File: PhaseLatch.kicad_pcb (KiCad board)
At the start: 4 copper layers, 68.8 x 53.6 mm, 120 parts, among them J2 NC, J20 I_IN, J21 Q_IN, J23 CLK_IN, J5 Databus, J6 Chip select, J7 Addressbus, J8 Signals, P1 Conn_02x10_Odd_Even, P2 Conn_02x10_Odd_Even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

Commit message: Ready for review
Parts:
- added C25: 100nF, Capacitor_SMD:C_0402_1005Metric, F.Cu at (170.2, 104.6)
- added C26: 100nF, Capacitor_SMD:C_0402_1005Metric, F.Cu at (149.4, 134.1)
- added C27: 100nF, Capacitor_SMD:C_0402_1005Metric, F.Cu at (139.2, 130.0)
- U2, U6, U7, U8: value TP74LVC1G132S5 -> SN74LVC1G132DCKR; footprint Package_TO_SOT_SMD:SOT-23-5 -> Package_TO_SOT_SMD:SOT-353_SC-70-5
- moved C21 20.9 mm to (155.5, 127.1)
- moved R26 1.44 mm to (142.0, 116.6), turned to -90 degrees
- moved C19 1.28 mm to (146.2, 119.8)
- moved R16 1.25 mm to (146.2, 120.8)
- moved C9 1.22 mm to (143.3, 119.3)
- moved R46 1.21 mm to (163.6, 112.5)
- moved R45 1.19 mm to (163.6, 113.4)
- moved R42 1.16 mm to (163.6, 116.2)
- moved R44 1.16 mm to (163.6, 114.3)
- moved R41 1.15 mm to (163.6, 117.2)
- moved R39 1.14 mm to (163.6, 119.1)
- moved R40 1.14 mm to (163.6, 118.2)
- moved R43 1.14 mm to (163.6, 115.3)
- moved C4 1.06 mm to (140.8, 120.2)
- moved C5 1.01 mm to (140.8, 119.2)
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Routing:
- net /"$0800": track 0.00 -> 35.5 mm, vias 0 -> 2
- net Net-(JP9-A): track 15.5 -> 37.9 mm
- net Net-(JP14-B): track 0.00 -> 21.0 mm, vias 0 -> 2
- net VCC: track 17.1 -> 33.7 mm, vias 12 -> 15
- net Net-(U4-~{OE}): track 5.51 -> 19.8 mm
- net +Ext_3V3: track 55.0 -> 69.2 mm
- net A6: track 55.6 -> 68.0 mm
- net GND: track 0.00 -> 7.29 mm, vias 42 -> 110
- net Net-(JP14-A): track 11.9 -> 14.6 mm
- net Net-(JP6-A): track 5.06 -> 7.39 mm
- net /PB2: track 20.7 -> 22.6 mm
- net Net-(JP6-B): track 17.7 -> 19.5 mm
- net Net-(U1-D1): track 3.13 -> 1.68 mm
- net Net-(U1-REFT-I): track 6.56 -> 8.00 mm
- net Net-(U1-D0): track 3.29 -> 1.87 mm
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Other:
- board text added: "A0"
- board text added: "A13"
- board text added: "A14"
- board text added: "CLK"

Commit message: Mods from review
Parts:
- moved JP4 0.89 mm to (164.8, 134.2)
- moved JP5 0.85 mm to (164.8, 132.2)
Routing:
- net A6: track 68.0 -> 51.6 mm, vias 1 -> 2
- net D2: track 46.6 -> 49.2 mm
- net D1: track 49.9 -> 51.8 mm
- net VCC: track 33.7 -> 32.2 mm
- net Net-(U4-~{WE}): track 28.8 -> 30.4 mm
- net Net-(JP2-B): track 16.1 -> 14.8 mm
- net D3: track 51.9 -> 53.1 mm
- net A0: track 58.4 -> 59.4 mm
- net /PB2: track 22.6 -> 21.6 mm
- net D5: track 50.7 -> 49.7 mm
- net Net-(JP5-A): track 2.87 -> 2.02 mm
- net /A13: track 99.3 -> 100.0 mm
- net D0: track 47.1 -> 47.6 mm
- net GND: vias 110 -> 144

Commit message: Final touches
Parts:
- moved C21 4.72 mm to (150.8, 126.9)
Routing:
- net Net-(U4-~{WE}): track 30.4 -> 27.7 mm
- net /A13: track 100.0 -> 98.2 mm
- net VCC: track 32.2 -> 33.9 mm
- net Net-(JP1-C): track 4.66 -> 5.40 mm
- net GND: vias 144 -> 168
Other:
- board text added: "S"
- board text added: "VDD"

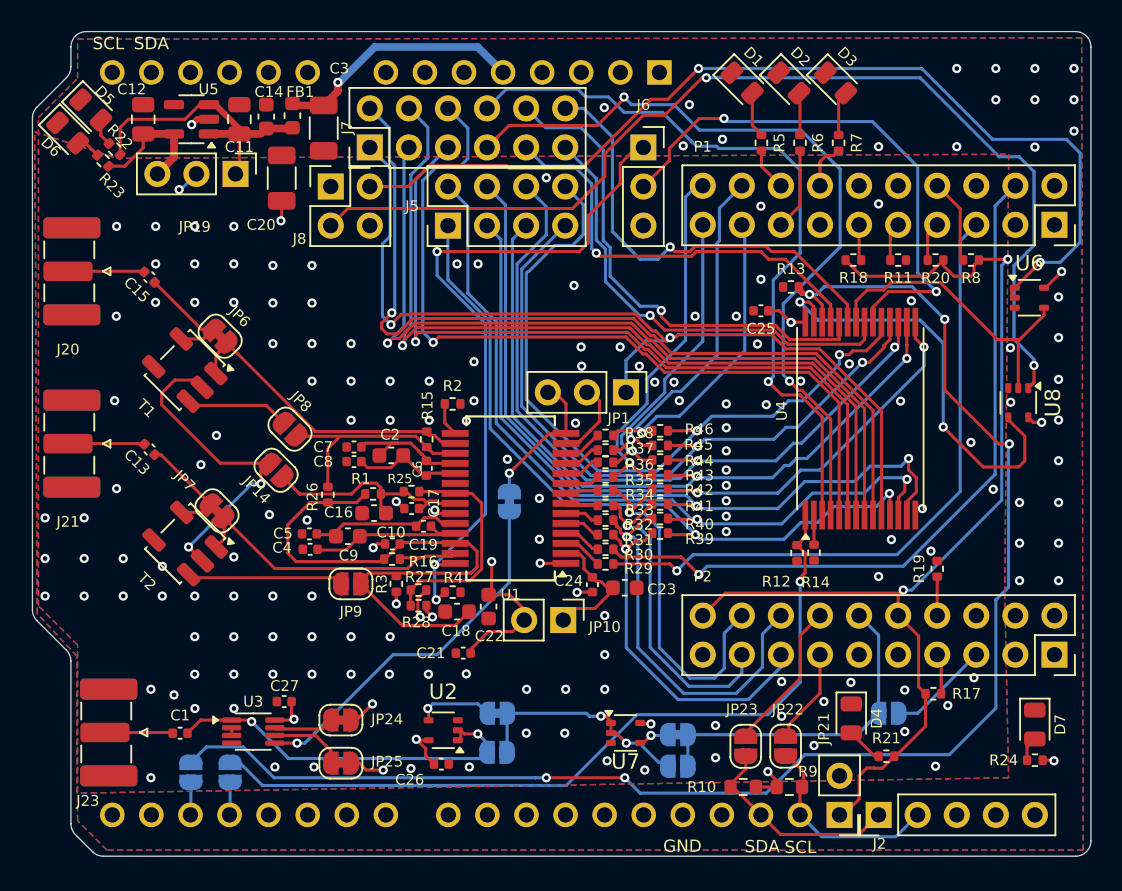
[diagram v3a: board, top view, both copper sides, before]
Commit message: Version 1.1 - correct RAM footprint
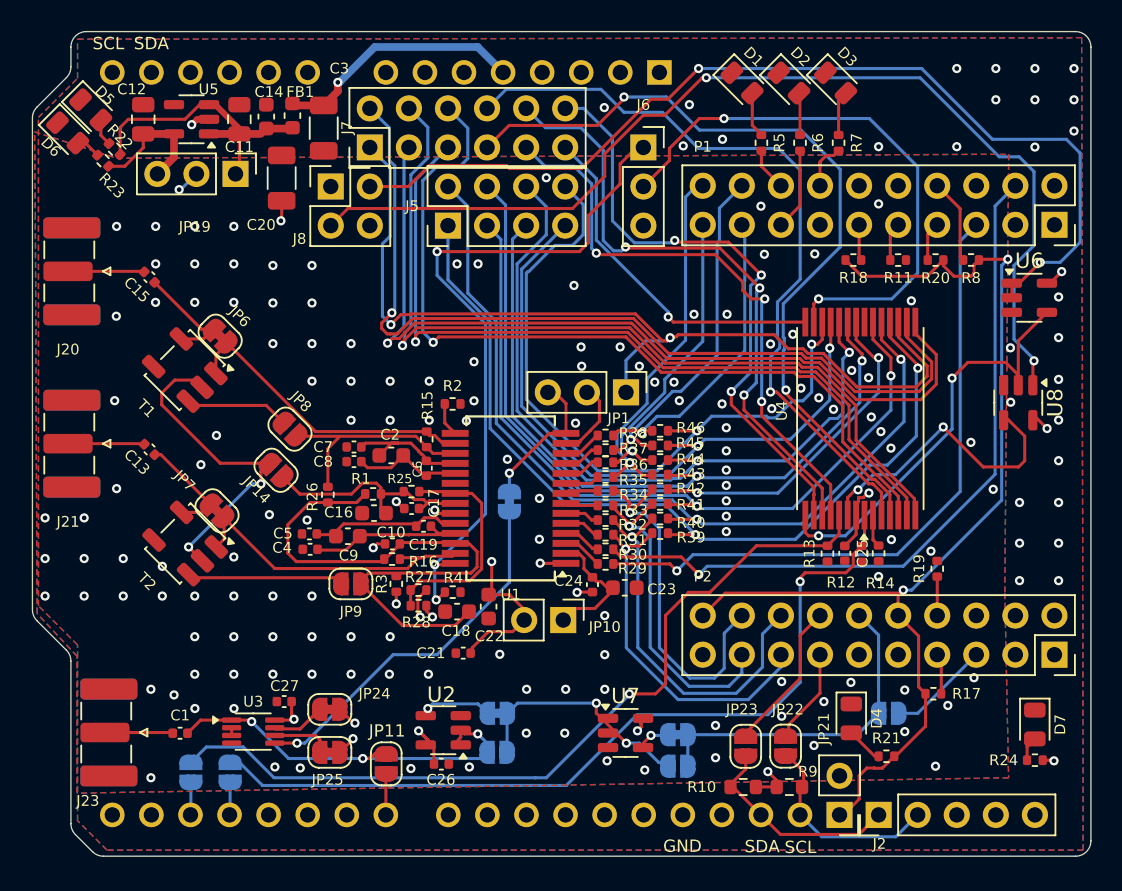
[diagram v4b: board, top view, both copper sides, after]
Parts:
- added JP11: SolderJumper_2_Open, Jumper:SolderJumper-2_P1.3mm_Open_RoundedPad1.0x1.5mm, F.Cu at (145.8, 134.1)
- U2, U6, U7, U8: footprint Package_TO_SOT_SMD:SOT-353_SC-70-5 -> Package_TO_SOT_SMD:SOT-23-5
- moved R13 17.5 mm to (174.5, 120.4), turned to 90 degrees
- moved C25 16.7 mm to (175.6, 120.4), turned to -90 degrees
- moved R14 4.20 mm to (177.8, 120.4)
- moved R12 4.20 mm to (176.7, 120.4)
- moved JP25 1.01 mm to (142.1, 133.3)
- moved JP24 1.01 mm to (142.1, 130.6)
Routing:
- net /A13: track 98.2 -> 53.8 mm, vias 5 -> 1
- net A8: track 27.9 -> 38.4 mm, vias 1 -> 3
- net D0: track 47.6 -> 57.7 mm
- net A11: track 29.3 -> 39.2 mm, vias 1 -> 3
- net Net-(U4-~{WE}): track 27.7 -> 19.2 mm
- net A9: track 32.5 -> 41.0 mm, vias 1 -> 3
- net Net-(U4-~{OE}): track 19.8 -> 28.2 mm, vias 0 -> 2
- net A10: track 29.6 -> 22.8 mm
- net D1: track 51.8 -> 57.6 mm
- net USRLED4: track 0.00 -> 2.51 mm
- net D2: track 49.2 -> 51.4 mm
- net D7: track 48.4 -> 46.2 mm
- net /A14: track 51.9 -> 54.0 mm
- net A2: track 53.6 -> 55.4 mm
- net A5: track 53.7 -> 55.4 mm
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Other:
- board text added: "v1.1"
- board text removed: "v1.0"
